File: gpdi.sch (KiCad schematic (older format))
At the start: 21 parts, among them U1 LFE5U-85F-6BG381C, U11 PCA9306D

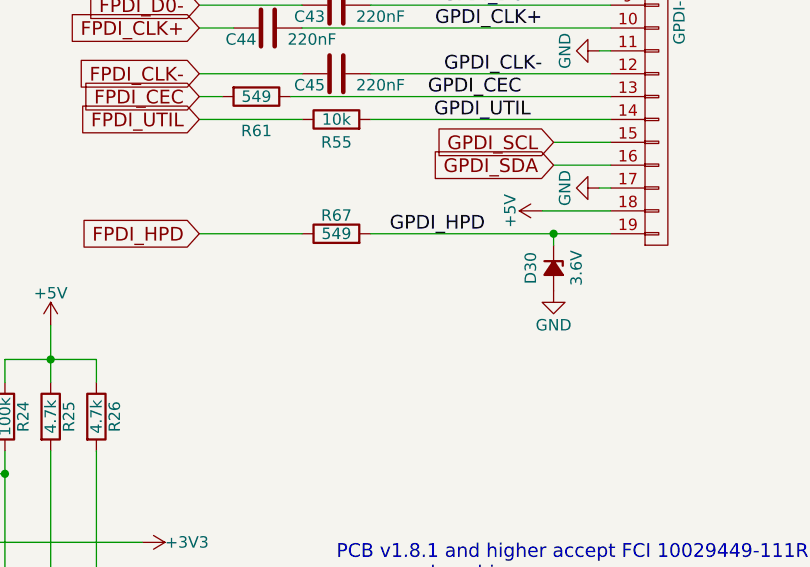
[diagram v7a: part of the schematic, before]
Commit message: schematics: fix wrong placed zener D30 at gpdi
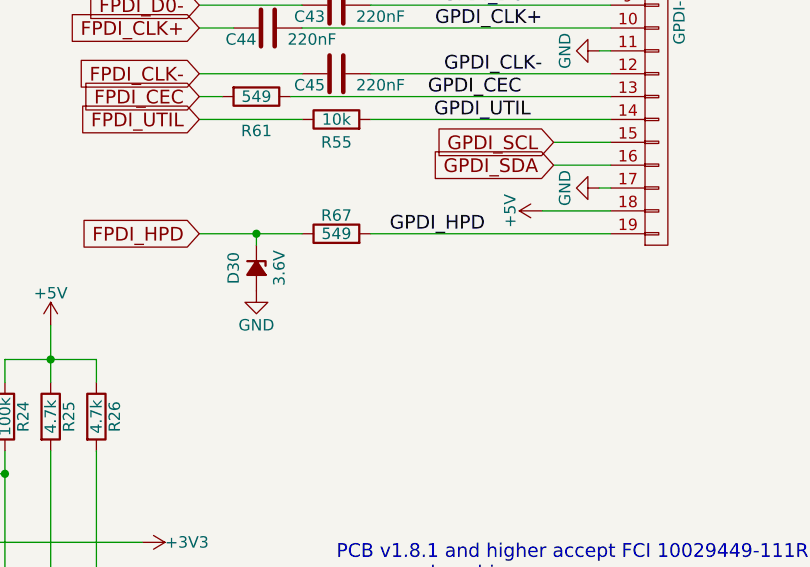
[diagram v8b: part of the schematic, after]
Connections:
- net FPDI_HPD: now also D30.1 (K)
- net GPDI_HPD: no longer D30.1 (K)
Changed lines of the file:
@@
 	0    1    -1   0
-$EndComp
-$Comp
-L power:+5V #PWR095
-U 1 1 58D6907F
-P 8450 3800
-F 0 "#PWR095" H 8450 3650 50  0001 C CNN
-F 1 "+5V" H 8450 3940 50  0000 C CNN
-F 2 "" H 8450 3800 50  0000 C CNN
-F 3 "" H 8450 3800 50  0000 C CNN
-	1    8450 3800
-	0    -1   1    0
 $EndComp
 Text GLabel 6950 3900 0    60   Input ~ 0
@@
 	8750 3700 8700 3700
 Wire Wire Line
-	8750 3900 8500 3900
-Wire Wire Line
 	8750 3800 8450 3800
 Wire Wire Line
@@
 	7400 2300 6950 2300
 Wire Wire Line
-	7400 3900 6950 3900
+	7400 3900 7200 3900
 Wire Wire Line
 	7100 3000 6950 3000
@@
 GPDI_CEC
 $Comp
-L Device:D_Zener_Small_ALT D?
-U 1 1 5F8E4470
-P 8500 4050
-AR Path="/58D6BF46/5F8E4470" Ref="D?"  Part="1"
-AR Path="/58D686D9/5F8E4470" Ref="D30"  Part="1"
-F 0 "D30" H 8500 3950 50  0000 C CNN
-F 1 "3.6V" H 8500 4150 50  0000 C CNN
-F 2 "Diode_SMD:D_SOD-323_HandSoldering" V 8500 4050 50  0001 C CNN
-F 3 "http://www.taiwansemi.com/products/datasheet/BZT52C2V4S%20SERIES_H1709.pdf" V 8500 4050 50  0001 C CNN
-	1    8500 4050
-	0    1    1    0
-$EndComp
-Wire Wire Line
-	8500 3900 8500 3950
-Connection ~ 8500 3900
-Wire Wire Line
-	8500 3900 7700 3900
-$Comp
-L power:GND #PWR043
-U 1 1 5F8F4E63
-P 8500 4150
-F 0 "#PWR043" H 8500 3900 50  0001 C CNN
-F 1 "GND" H 8500 4000 50  0000 C CNN
-F 2 "" H 8500 4150 50  0000 C CNN
-F 3 "" H 8500 4150 50  0000 C CNN
-	1    8500 4150
-	1    0    0    -1
-$EndComp
-$Comp
 L Device:R R55
 U 1 1 5F9109EC
@@
 	0    -1   -1   0
 $EndComp
+$Comp
+L power:+5V #PWR095
+U 1 1 58D6907F
+P 8450 3800
+F 0 "#PWR095" H 8450 3650 50  0001 C CNN
+F 1 "+5V" H 8450 3940 50  0000 C CNN
+F 2 "" H 8450 3800 50  0000 C CNN
+F 3 "" H 8450 3800 50  0000 C CNN
+	1    8450 3800
+	0    -1   1    0
+$EndComp
+Wire Wire Line
+	7700 3900 8750 3900
+$Comp
+L power:GND #PWR?
+U 1 1 5F8E2751
+P 7200 4150
+F 0 "#PWR?" H 7200 3900 50  0001 C CNN
+F 1 "GND" H 7200 4000 50  0000 C CNN
+F 2 "" H 7200 4150 50  0000 C CNN
+F 3 "" H 7200 4150 50  0000 C CNN
+	1    7200 4150
+	1    0    0    -1
+$EndComp
+Wire Wire Line
+	7200 3900 7200 3950
+$Comp
+L Device:D_Zener_Small_ALT D?
+U 1 1 5F8E2758
+P 7200 4050
+AR Path="/58D6BF46/5F8E2758" Ref="D?"  Part="1"
+AR Path="/58D686D9/5F8E2758" Ref="D30"  Part="1"
+F 0 "D30" H 7200 3950 50  0000 C CNN
+F 1 "3.6V" H 7200 4150 50  0000 C CNN
+F 2 "Diode_SMD:D_SOD-323_HandSoldering" V 7200 4050 50  0001 C CNN
+F 3 "http://www.taiwansemi.com/products/datasheet/BZT52C2V4S%20SERIES_H1709.pdf" V 7200 4050 50  0001 C CNN
+	1    7200 4050
+	0    1    1    0
+$EndComp
+Connection ~ 7200 3900
+Wire Wire Line
+	7200 3900 6950 3900
 $EndSCHEMATC
